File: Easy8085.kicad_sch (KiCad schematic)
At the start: 35 parts, among them J1 Expansion, J2 5V Power, J3 FTDI, SW1 RESET, U1 8085, U2 8251A, U3 74LS90, U4 74LS139, U5 74LS573, U6 CY62256, U7 X28256, Y1 6.144M

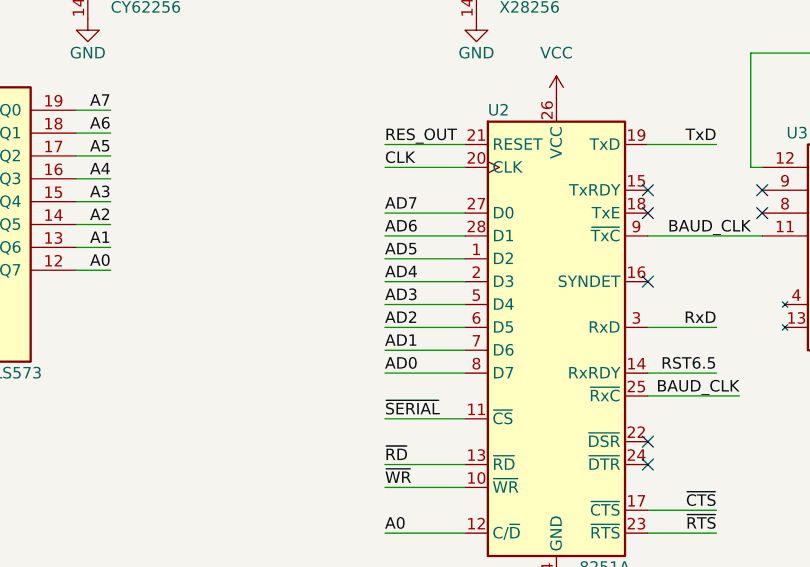
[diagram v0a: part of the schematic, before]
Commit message: Found and fixed error with AD0-7 reversed on UART
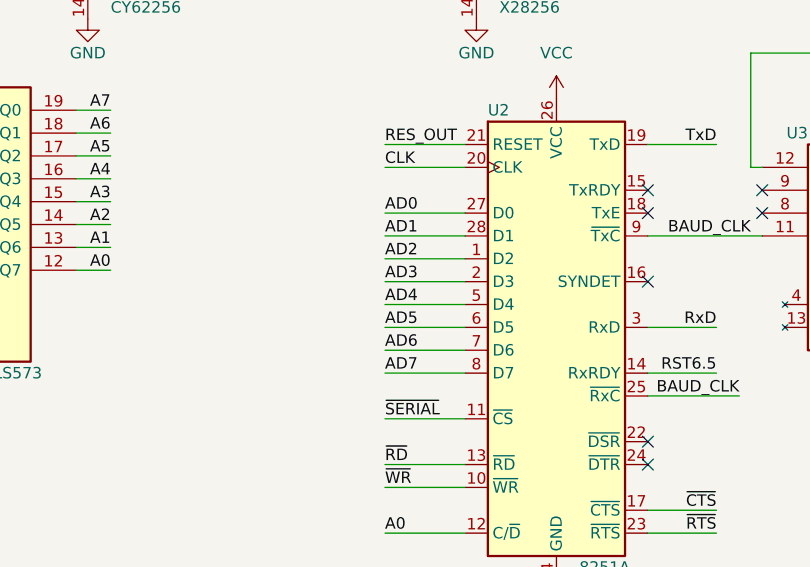
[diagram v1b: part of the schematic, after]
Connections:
- net AD0: now also U2.27 (D0); no longer U2.8 (D7)
- net AD1: now also U2.28 (D1); no longer U2.7 (D6)
- net AD2: now also U2.1 (D2); no longer U2.6 (D5)
- net AD3: now also U2.2 (D3); no longer U2.5 (D4)
- net AD4: now also U2.5 (D4); no longer U2.2 (D3)
- net AD5: now also U2.6 (D5); no longer U2.1 (D2)
- net AD6: now also U2.7 (D6); no longer U2.28 (D1)
- net AD7: now also U2.8 (D7); no longer U2.27 (D0)
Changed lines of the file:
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@@
     (effects (font (size 1.27 1.27)) (justify left bottom))
   )
-  (label "AD2" (at 208.28 99.06 0)
-    (effects (font (size 1.27 1.27)) (justify left bottom))
-  )
-  (label "AD7" (at 208.28 86.36 0)
+  (label "AD2" (at 208.28 91.44 0)
+    (effects (font (size 1.27 1.27)) (justify left bottom))
+  )
+  (label "AD7" (at 208.28 104.14 0)
     (effects (font (size 1.27 1.27)) (justify left bottom))
   )
@@
     (effects (font (size 1.27 1.27)) (justify right bottom))
   )
-  (label "AD0" (at 208.28 104.14 0)
+  (label "AD0" (at 208.28 86.36 0)
     (effects (font (size 1.27 1.27)) (justify left bottom))
   )
@@
     (effects (font (size 1.27 1.27)) (justify left bottom))
   )
-  (label "AD4" (at 208.28 93.98 0)
+  (label "AD4" (at 208.28 96.52 0)
     (effects (font (size 1.27 1.27)) (justify left bottom))
   )
@@
     (effects (font (size 1.27 1.27)) (justify right bottom))
   )
-  (label "AD1" (at 208.28 101.6 0)
+  (label "AD1" (at 208.28 88.9 0)
     (effects (font (size 1.27 1.27)) (justify left bottom))
   )
@@
     (effects (font (size 1.27 1.27)) (justify left bottom))
   )
-  (label "AD3" (at 208.28 96.52 0)
+  (label "AD3" (at 208.28 93.98 0)
     (effects (font (size 1.27 1.27)) (justify left bottom))
   )
@@
     (effects (font (size 1.27 1.27)) (justify right bottom))
   )
-  (label "AD6" (at 208.28 88.9 0)
+  (label "AD6" (at 208.28 101.6 0)
     (effects (font (size 1.27 1.27)) (justify left bottom))
   )
@@
     (effects (font (size 1.27 1.27)) (justify right bottom))
   )
-  (label "AD5" (at 208.28 91.44 0)
-    (effects (font (size 1.27 1.27)) (justify left bottom))
-  )
+  (label "AD5" (at 208.28 99.06 0)
+    (effects (font (size 1.27 1.27)) (justify left bottom))
+  )
